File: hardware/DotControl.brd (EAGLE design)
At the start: 30.7 x 65 mm, 32 parts, among them CN1 1X4-BIG, J3 USB-MICROB, SW2 Previous, SW5 Previous, SW6 Next, SW8 Ok, U1 ATMEGA328P-MU-QFN32, U2 TMP102, U3 ATSHA204-TSU

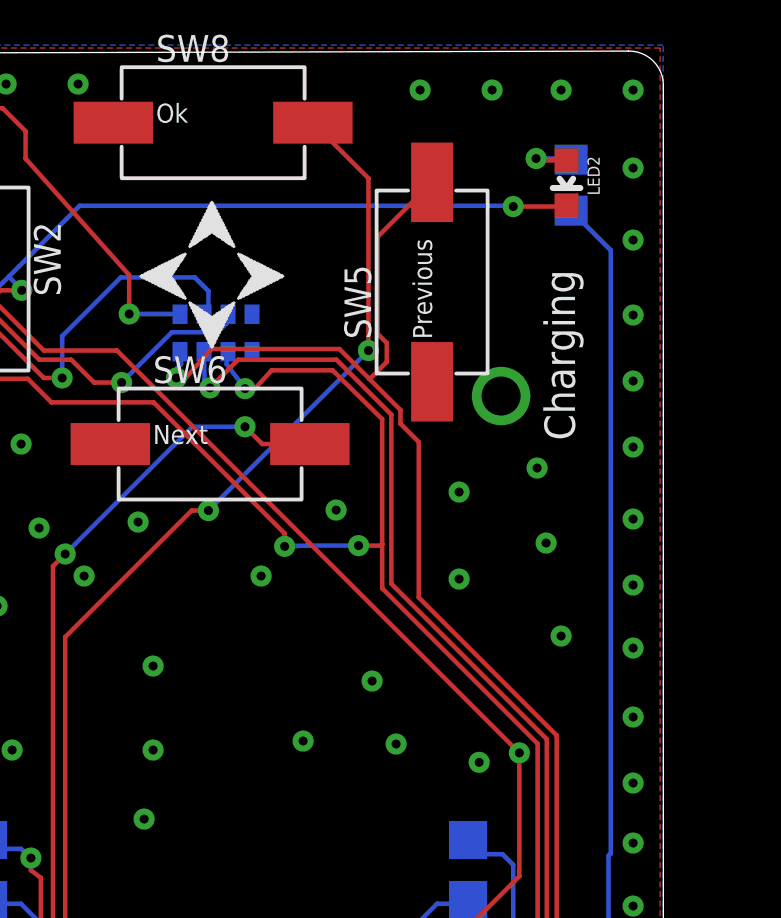
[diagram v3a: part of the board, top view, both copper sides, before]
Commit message: Swap R with B @ pushbutton
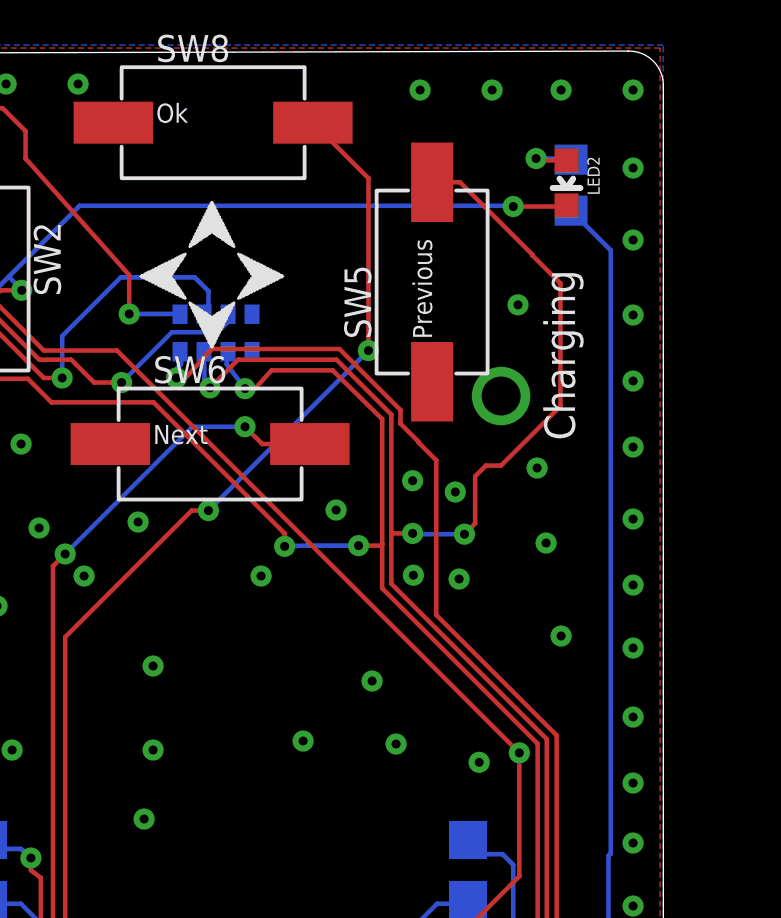
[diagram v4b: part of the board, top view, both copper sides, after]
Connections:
- net LED: no longer SW5.2
- net RXD: now also SW5.2
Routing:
- net RXD: track 48.0 -> 66.1 mm, vias 2 -> 4
- net LED: track 69.3 -> 61.6 mm
- net GND: vias 104 -> 107
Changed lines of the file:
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@@
 <via x="25.2" y="21.3" extent="1-16" drill="0.3"/>
 <via x="23.9" y="47.4" extent="1-16" drill="0.3"/>
-<via x="23.9" y="50.3" extent="1-16" drill="0.3"/>
+<via x="23.773" y="50.3" extent="1-16" drill="0.3"/>
 <via x="26.5" y="51.1" extent="1-16" drill="0.3"/>
 <via x="26.8" y="48.6" extent="1-16" drill="0.3"/>
@@
 <contactref element="X1" pad="1"/>
 <contactref element="X1" pad="2"/>
+<via x="22.3506" y="50.6766" extent="1-16" drill="0.3"/>
+<via x="22.376" y="47.527" extent="1-16" drill="0.3"/>
+<via x="25.8646" y="56.54" extent="1-16" drill="0.3"/>
 <wire x1="16.256" y1="17.85" x2="16.1798" y2="17.8308" width="0" layer="19" extent="16-16"/>
 <wire x1="3.9624" y1="28.0958" x2="3.9624" y2="25.3458" width="0" layer="19" extent="1-1"/>
@@
 <wire x1="15.6464" y1="55.0672" x2="14.7828" y2="54.102" width="0.1524" layer="1"/>
 <wire x1="19.9136" y1="55.0672" x2="15.6464" y2="55.0672" width="0.1524" layer="1"/>
-<wire x1="21.9456" y1="53.0352" x2="20.9169" y2="54.0639" width="0.1524" layer="1"/>
-<wire x1="20.9169" y1="54.0639" x2="19.9136" y2="55.0672" width="0.1524" layer="1"/>
+<wire x1="21.9456" y1="53.0352" x2="19.9136" y2="55.0672" width="0.1524" layer="1"/>
 <wire x1="21.9456" y1="52.578" x2="21.9456" y2="53.0352" width="0.1524" layer="1"/>
 <wire x1="22.5552" y1="51.9684" x2="21.9456" y2="52.578" width="0.1524" layer="1"/>
-<wire x1="22.5552" y1="46.7868" x2="22.5552" y2="51.9684" width="0.1524" layer="1"/>
-<wire x1="27.1526" y1="42.1894" x2="22.5552" y2="46.7868" width="0.1524" layer="1"/>
+<wire x1="27.1526" y1="42.1894" x2="23.1394" y2="46.2026" width="0.1524" layer="1"/>
 <wire x1="24.384" y1="22.098" x2="26.0604" y2="23.7744" width="0.1524" layer="16"/>
 <wire x1="24.384" y1="16.3068" x2="24.384" y2="22.098" width="0.1524" layer="16"/>
@@
 <wire x1="25.3238" y1="30.7848" x2="27.1526" y2="32.6136" width="0.1524" layer="1"/>
 <wire x1="27.1526" y1="32.6136" x2="27.1526" y2="42.1894" width="0.1524" layer="1"/>
-<contactref element="SW5" pad="2"/>
-<wire x1="23" y1="60.625" x2="21.1836" y2="58.8086" width="0.1524" layer="1"/>
-<wire x1="21.1836" y1="58.8086" x2="21.1836" y2="55.5752" width="0.1524" layer="1"/>
-<wire x1="21.1836" y1="55.5752" x2="21.4884" y2="55.2704" width="0.1524" layer="1"/>
-<wire x1="21.4884" y1="55.2704" x2="21.4884" y2="54.6354" width="0.1524" layer="1"/>
-<wire x1="21.4884" y1="54.6354" x2="20.9169" y2="54.0639" width="0.1524" layer="1"/>
+<wire x1="22.5552" y1="51.9684" x2="22.5552" y2="51.943" width="0.1524" layer="1"/>
+<wire x1="22.5552" y1="51.943" x2="23.1394" y2="51.3588" width="0.1524" layer="1"/>
+<wire x1="23.1394" y1="51.3588" x2="23.1394" y2="46.2026" width="0.1524" layer="1"/>
 </signal>
 <signal name="LIGHT_SENSE">
@@
 <wire x1="19.812" y1="54.7116" x2="16.5354" y2="54.7116" width="0.1524" layer="1"/>
 <wire x1="21.6408" y1="52.8828" x2="19.812" y2="54.7116" width="0.1524" layer="1"/>
-<wire x1="21.6408" y1="47.244" x2="21.6408" y2="52.8828" width="0.1524" layer="1"/>
+<wire x1="21.6408" y1="47.244" x2="21.6408" y2="48.9712" width="0.1524" layer="1"/>
+<wire x1="21.6408" y1="48.9712" x2="21.6408" y2="52.8828" width="0.1524" layer="1"/>
 <wire x1="26.8224" y1="42.0624" x2="21.6408" y2="47.244" width="0.1524" layer="1"/>
 <wire x1="26.8224" y1="32.766" x2="26.8224" y2="42.0624" width="0.1524" layer="1"/>
@@
 <via x="15.5956" y="53.7718" extent="1-16" drill="0.3"/>
 <via x="17.526" y="23.4696" extent="1-16" drill="0.3"/>
+<contactref element="SW5" pad="2"/>
+<wire x1="24.4348" y1="50.8254" x2="24.4348" y2="49.2506" width="0.1524" layer="1"/>
+<wire x1="24.4348" y1="49.2506" x2="24.0792" y2="48.895" width="0.1524" layer="1"/>
+<via x="24.0792" y="48.895" extent="1-16" drill="0.3"/>
+<wire x1="24.0792" y1="48.895" x2="22.3774" y2="48.895" width="0.1524" layer="16"/>
+<wire x1="22.3774" y1="48.895" x2="22.352" y2="48.9204" width="0.1524" layer="16"/>
+<via x="22.352" y="48.9204" extent="1-16" drill="0.3"/>
+<wire x1="22.352" y1="48.9204" x2="21.6916" y2="48.9204" width="0.1524" layer="1"/>
+<wire x1="21.6916" y1="48.9204" x2="21.6408" y2="48.9712" width="0.1524" layer="1"/>
+<wire x1="23" y1="60.625" x2="23.9316" y2="60.625" width="0.1524" layer="1"/>
+<wire x1="23.9316" y1="60.625" x2="26.3398" y2="58.2168" width="0.1524" layer="1"/>
+<wire x1="26.3398" y1="58.2168" x2="26.3398" y2="58.1914" width="0.1524" layer="1"/>
+<wire x1="26.3398" y1="58.1914" x2="27.2796" y2="57.2516" width="0.1524" layer="1"/>
+<wire x1="27.2796" y1="57.2516" x2="27.2796" y2="53.1622" width="0.1524" layer="1"/>
+<wire x1="27.2796" y1="53.1622" x2="25.2984" y2="51.181" width="0.1524" layer="1"/>
+<wire x1="25.2984" y1="51.181" x2="24.7904" y2="51.181" width="0.1524" layer="1"/>
+<wire x1="24.7904" y1="51.181" x2="24.4348" y2="50.8254" width="0.1524" layer="1"/>
 </signal>
 <signal name="ADC">

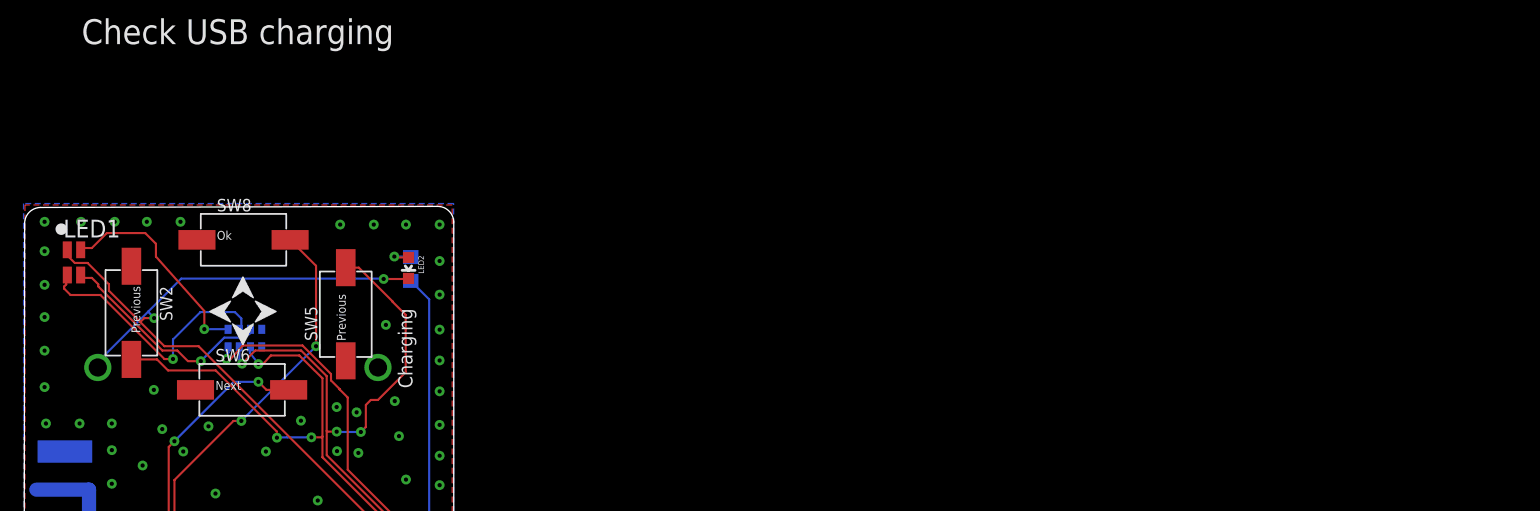
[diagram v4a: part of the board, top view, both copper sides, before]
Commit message: Light RGB composite colors on push press
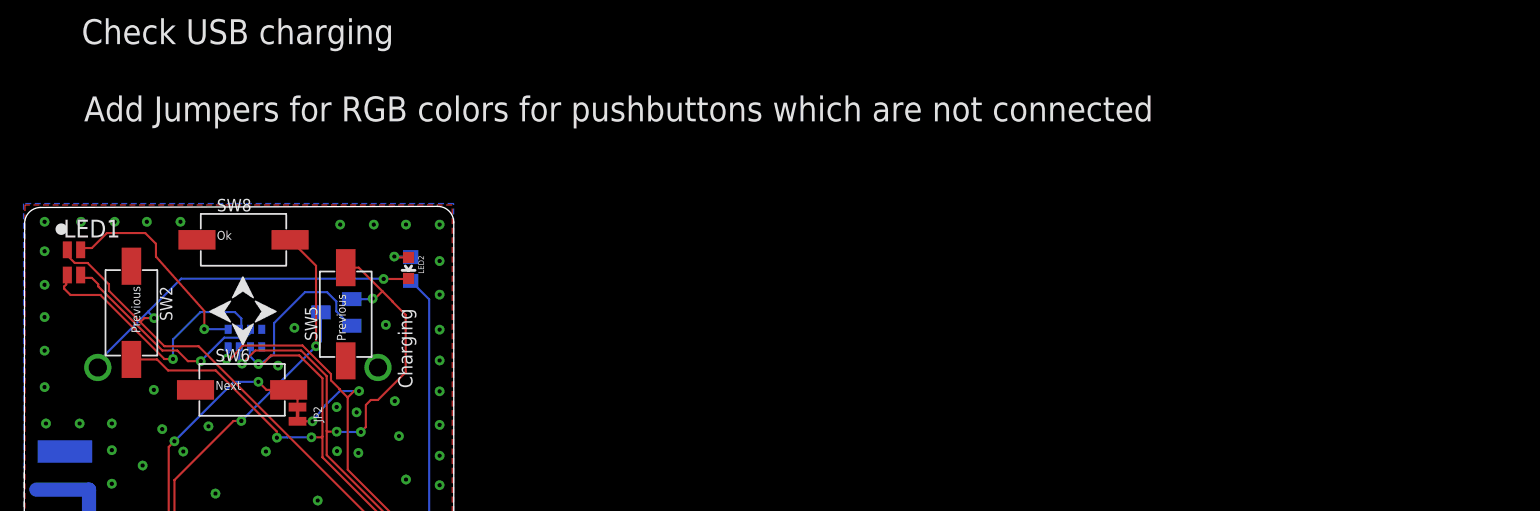
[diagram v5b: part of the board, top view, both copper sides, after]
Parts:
- added D4: BAS70-05, diode:SOT23
- added JP2: JUMPER-SMT_2_NC_TRACE_NO-SILK, SparkFun-Jumpers:SMT-JUMPER_2_NC_TRACE_NO-SILK
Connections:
- net N$10 renamed BLUE
- net N$15 renamed RED
- net N$9 renamed GREEN
- net ADCENA: now also JP2.1
- net BUZZER: now also D4.3
- net LED: now also JP2.2
- net RXD: now also D4.1
- net TXD: now also D4.2
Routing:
- net TXD: track 62.4 -> 74.1 mm
- net LED: track 61.6 -> 67.9 mm, vias 2 -> 4
- net BUZZER: track 50.4 -> 53.0 mm
- net RXD: track 66.1 -> 68.5 mm, vias 4 -> 5
- net ADCENA: track 77.4 -> 78.9 mm
- net GND: vias 107 -> 108
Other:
- board text added: "Add Jumpers for RGB colors for pushbuttons which are not connected"
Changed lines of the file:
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@@
 <rectangle x1="0.1524" y1="25.527" x2="5.6134" y2="48.9712" layer="42"/>
 <text x="4.1402" y="76.581" size="1.778" layer="21">Check USB charging</text>
+<text x="4.318" y="71.0692" size="1.778" layer="21">Add Jumpers for RGB colors for pushbuttons which are not connected</text>
 </plain>
 <attributes>
@@
 <element name="R5" library="rcl" package="R0603" value="" x="27.8638" y="32.6644" rot="MR90"/>
 <element name="X1" library="adafruit" package="U.FL" value="" x="3.9624" y="26.7208"/>
+<element name="D4" library="diode" package="SOT23" value="BAS70-05" x="22.3266" y="57.4294" rot="MR270"/>
+<element name="JP2" library="SparkFun-Jumpers" package="SMT-JUMPER_2_NC_TRACE_NO-SILK" value="JUMPER-SMT_2_NC_TRACE_NO-SILK" x="19.558" y="50.165" rot="R270"/>
 </elements>
 <signals>
@@
 <wire x1="15.85" y1="18.85" x2="15.1" y2="18.1" width="0.1524" layer="16"/>
 <via x="9.3" y="51.9" extent="1-16" drill="0.3"/>
-<via x="19.8" y="49.7" extent="1-16" drill="0.3"/>
 <via x="23.1" y="16.4" extent="1-16" drill="0.3"/>
 <wire x1="23.1" y1="16.4" x2="22.9" y2="16.6" width="0.1524" layer="16"/>
@@
 <via x="22.376" y="47.527" extent="1-16" drill="0.3"/>
 <via x="25.8646" y="56.54" extent="1-16" drill="0.3"/>
+<via x="19.3368" y="56.327" extent="1-16" drill="0.3"/>
+<via x="18.1684" y="53.6346" extent="1-16" drill="0.3"/>
 <wire x1="16.256" y1="17.85" x2="16.1798" y2="17.8308" width="0" layer="19" extent="16-16"/>
 <wire x1="3.9624" y1="28.0958" x2="3.9624" y2="25.3458" width="0" layer="19" extent="1-1"/>
@@
 <wire x1="19.6596" y1="22.86" x2="16.9164" y2="22.86" width="0.1524" layer="1"/>
 <wire x1="19.9644" y1="23.1648" x2="19.6596" y2="22.86" width="0.1524" layer="1"/>
-<wire x1="25.7556" y1="23.1648" x2="19.9644" y2="23.1648" width="0.1524" layer="1"/>
 <wire x1="28.3464" y1="20.574" x2="25.7556" y2="23.1648" width="0.1524" layer="1"/>
 <wire x1="28.3464" y1="6.7056" x2="28.3464" y2="14.478" width="0.1524" layer="1"/>
@@
 <wire x1="26.162" y1="6.1976" x2="27.8384" y2="6.1976" width="0.1524" layer="1"/>
 <wire x1="27.8384" y1="6.1976" x2="28.3464" y2="6.7056" width="0.1524" layer="1"/>
+<wire x1="25.7556" y1="23.1648" x2="19.9644" y2="23.1648" width="0.1524" layer="1"/>
 </signal>
 <signal name="+3V3">
@@
 <wire x1="18.5166" y1="20.7772" x2="19.3802" y2="20.7772" width="0.1524" layer="16"/>
 <via x="19.3802" y="20.7772" extent="1-16" drill="0.3"/>
-<wire x1="19.3802" y1="20.7772" x2="24.7396" y2="20.7772" width="0.1524" layer="1"/>
 <wire x1="24.7396" y1="20.7772" x2="24.7904" y2="20.7264" width="0.1524" layer="1"/>
 <wire x1="24.7904" y1="20.7264" x2="24.7904" y2="20.4978" width="0.1524" layer="1"/>
@@
 <wire x1="22.0218" y1="13.8176" x2="22.0218" y2="6.9718" width="0.1524" layer="16"/>
 <wire x1="22.0218" y1="6.9718" x2="21.35" y2="6.3" width="0.1524" layer="16"/>
+<wire x1="19.3802" y1="20.7772" x2="24.7396" y2="20.7772" width="0.1524" layer="1"/>
 </signal>
 <signal name="+5V">
@@
 <wire x1="22.5552" y1="51.943" x2="23.1394" y2="51.3588" width="0.1524" layer="1"/>
 <wire x1="23.1394" y1="51.3588" x2="23.1394" y2="46.2026" width="0.1524" layer="1"/>
+<contactref element="JP2" pad="2"/>
+<via x="20.6248" y="49.657" extent="1-16" drill="0.3"/>
+<wire x1="20.6248" y1="49.657" x2="21.5392" y2="50.8" width="0.1524" layer="16"/>
+<wire x1="21.5392" y1="50.8" x2="22.5806" y2="51.816" width="0.1524" layer="16"/>
+<wire x1="22.5806" y1="51.816" x2="23.9522" y2="51.816" width="0.1524" layer="16"/>
+<via x="23.9522" y="51.816" extent="1-16" drill="0.3"/>
+<wire x1="23.9522" y1="51.816" x2="23.5966" y2="51.816" width="0.1524" layer="1"/>
+<wire x1="23.5966" y1="51.816" x2="23.1394" y2="51.3588" width="0.1524" layer="1"/>
+<wire x1="20.6248" y1="49.657" x2="19.558" y2="49.657" width="0.1524" layer="1"/>
 </signal>
 <signal name="LIGHT_SENSE">
@@
 <via x="10.7696" y="48.2346" extent="1-16" drill="0.3"/>
 <wire x1="10.7696" y1="48.2346" x2="10.3632" y2="47.8282" width="0.1524" layer="1"/>
+<contactref element="JP2" pad="1"/>
+<wire x1="19.558" y1="50.673" x2="19.558" y2="51.267" width="0.1524" layer="1"/>
+<wire x1="19.558" y1="51.267" x2="18.925" y2="51.9" width="0.1524" layer="1"/>
 </signal>
 <signal name="TXD">
 <contactref element="U1" pad="31"/>
 <contactref element="R2" pad="2"/>
-<wire x1="16.1544" y1="54.5592" x2="16.1544" y2="54.864" width="0.1524" layer="16"/>
-<wire x1="16.764" y1="53.7464" x2="16.1544" y2="54.5592" width="0.1524" layer="16"/>
+<wire x1="16.1544" y1="54.3306" x2="16.1544" y2="54.864" width="0.1524" layer="16"/>
+<wire x1="16.764" y1="53.7464" x2="16.751809375" y2="53.66105625" width="0.1524" layer="16"/>
+<wire x1="16.751809375" y1="53.66105625" x2="16.1544" y2="54.3306" width="0.1524" layer="16"/>
 <wire x1="19.685" y1="54.356" x2="17.653" y2="54.356" width="0.1524" layer="1"/>
 <wire x1="17.653" y1="54.356" x2="17.0942" y2="53.7464" width="0.1524" layer="1"/>
@@
 <wire x1="18.0848" y1="48.4886" x2="18.2118" y2="48.3362" width="0.1524" layer="1"/>
 <wire x1="18.2118" y1="48.3362" x2="18.0848" y2="48.4632" width="0.1524" layer="1"/>
+<contactref element="D4" pad="2"/>
+<wire x1="23.4266" y1="56.4794" x2="23.3528" y2="56.4794" width="0.1524" layer="16"/>
+<wire x1="23.3528" y1="56.4794" x2="22.3266" y2="57.5056" width="0.1524" layer="16"/>
+<wire x1="22.3266" y1="57.5056" x2="22.3266" y2="58.2168" width="0.1524" layer="16"/>
+<wire x1="22.3266" y1="58.2168" x2="21.6662" y2="58.8772" width="0.1524" layer="16"/>
+<wire x1="21.6662" y1="58.8772" x2="20.0914" y2="58.8772" width="0.1524" layer="16"/>
+<wire x1="20.0914" y1="58.8772" x2="17.8816" y2="56.6674" width="0.1524" layer="16"/>
+<wire x1="17.8816" y1="56.6674" x2="17.8816" y2="54.460646875" width="0.1524" layer="16"/>
+<wire x1="17.8816" y1="54.460646875" x2="16.751809375" y2="53.66105625" width="0.1524" layer="16"/>
 </signal>
 <signal name="RXD">
@@
 <wire x1="21.6916" y1="48.9204" x2="21.6408" y2="48.9712" width="0.1524" layer="1"/>
 <wire x1="23" y1="60.625" x2="23.9316" y2="60.625" width="0.1524" layer="1"/>
-<wire x1="23.9316" y1="60.625" x2="26.3398" y2="58.2168" width="0.1524" layer="1"/>
+<wire x1="23.9316" y1="60.625" x2="25.6159" y2="58.9407" width="0.1524" layer="1"/>
+<wire x1="25.6159" y1="58.9407" x2="26.3398" y2="58.2168" width="0.1524" layer="1"/>
 <wire x1="26.3398" y1="58.2168" x2="26.3398" y2="58.1914" width="0.1524" layer="1"/>
 <wire x1="26.3398" y1="58.1914" x2="27.2796" y2="57.2516" width="0.1524" layer="1"/>
@@
 <wire x1="25.2984" y1="51.181" x2="24.7904" y2="51.181" width="0.1524" layer="1"/>
 <wire x1="24.7904" y1="51.181" x2="24.4348" y2="50.8254" width="0.1524" layer="1"/>
+<contactref element="D4" pad="1"/>
+<wire x1="23.4266" y1="58.3794" x2="24.9174" y2="58.3794" width="0.1524" layer="16"/>
+<wire x1="24.9174" y1="58.3794" x2="24.9174" y2="58.42" width="0.1524" layer="16"/>
+<via x="24.9174" y="58.42" extent="1-16" drill="0.3"/>
+<wire x1="24.9174" y1="58.42" x2="25.0952" y2="58.42" width="0.1524" layer="1"/>
+<wire x1="25.0952" y1="58.42" x2="25.6159" y2="58.9407" width="0.1524" layer="1"/>
 </signal>
 <signal name="ADC">
@@
 <wire x1="20.8788" y1="55.0164" x2="20.8788" y2="60.759" width="0.1524" layer="1"/>
 <wire x1="20.8788" y1="60.759" x2="19.0266" y2="62.6112" width="0.1524" layer="1"/>
+<contactref element="D4" pad="3"/>
+<wire x1="21.2266" y1="57.4294" x2="21.2266" y2="55.3642" width="0.1524" layer="16"/>
+<wire x1="21.2266" y1="55.3642" x2="20.8788" y2="55.0164" width="0.1524" layer="16"/>
 </signal>
 <signal name="OUTA">
@@
 <contactref element="JP1" pad="6"/>
 </signal>
-<signal name="N$9">
+<signal name="GREEN">
 <contactref element="LED1" pad="3"/>
 <contactref element="R2" pad="7"/>
@@
 <via x="12.6492" y="53.9496" extent="1-16" drill="0.3"/>
 </signal>
-<signal name="N$15">
+<signal name="RED">
 <contactref element="LED1" pad="1"/>
 <contactref element="R2" pad="5"/>
@@
 <via x="12.9032" y="56.2356" extent="1-16" drill="0.3"/>
 </signal>
-<signal name="N$10">
+<signal name="BLUE">
 <contactref element="LED1" pad="2"/>
 <contactref element="R2" pad="6"/>
@@
 <wire x1="27.8248" y1="26.6818" x2="27.1018" y2="25.9588" width="0.1524" layer="16"/>
 <wire x1="27.1018" y1="25.9588" x2="25.781" y2="25.9588" width="0.1524" layer="16"/>
-<wire x1="25.781" y1="25.9588" x2="24.4602" y2="24.638" width="0.1524" layer="16"/>
 <wire x1="24.4602" y1="24.638" x2="24.4602" y2="24.511" width="0.1524" layer="16"/>
 <wire x1="24.4602" y1="24.511" x2="23.9522" y2="24.003" width="0.1524" layer="16"/>
@@
 <via x="11.9126" y="27.4574" extent="1-16" drill="0.3"/>
 <wire x1="11.9126" y1="27.4574" x2="11.9126" y2="26.67" width="0.1524" layer="16"/>
+<wire x1="25.781" y1="25.9588" x2="24.4602" y2="24.638" width="0.1524" layer="16"/>
 </signal>
 <signal name="D+">
